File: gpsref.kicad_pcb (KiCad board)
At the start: 4 copper layers, 77.4 x 47.8 mm, 182 parts, among them J1 SMA, J10 Debug, J11 I2C_Snoop, J12 GPS_Snoop, J2 SMA, J3 SMA, J4 SMA, J5 U.Fl, J6 SMA, J7 USB_C_Receptacle_16P, J8 U.Fl, Q1 AO3400A, Q2 AO3401A, T1 MABA-007159-000000, T2 MABA-007159-000000, U1 MAX-M10S, U11 74LVC1G07, U2 LMK05318BRGZR, U21 TMP117xxDRV, U3 TG5032CGN, U31 74LVC1G125, U4 STM32H503KBUx, U41 74CB3Q3306, U5 TPS82084SIL, U6 TPS82084SIL, U7 TPS7A8801RTJR, U8 TPS7A8801RTJR, Y1 32768Hz

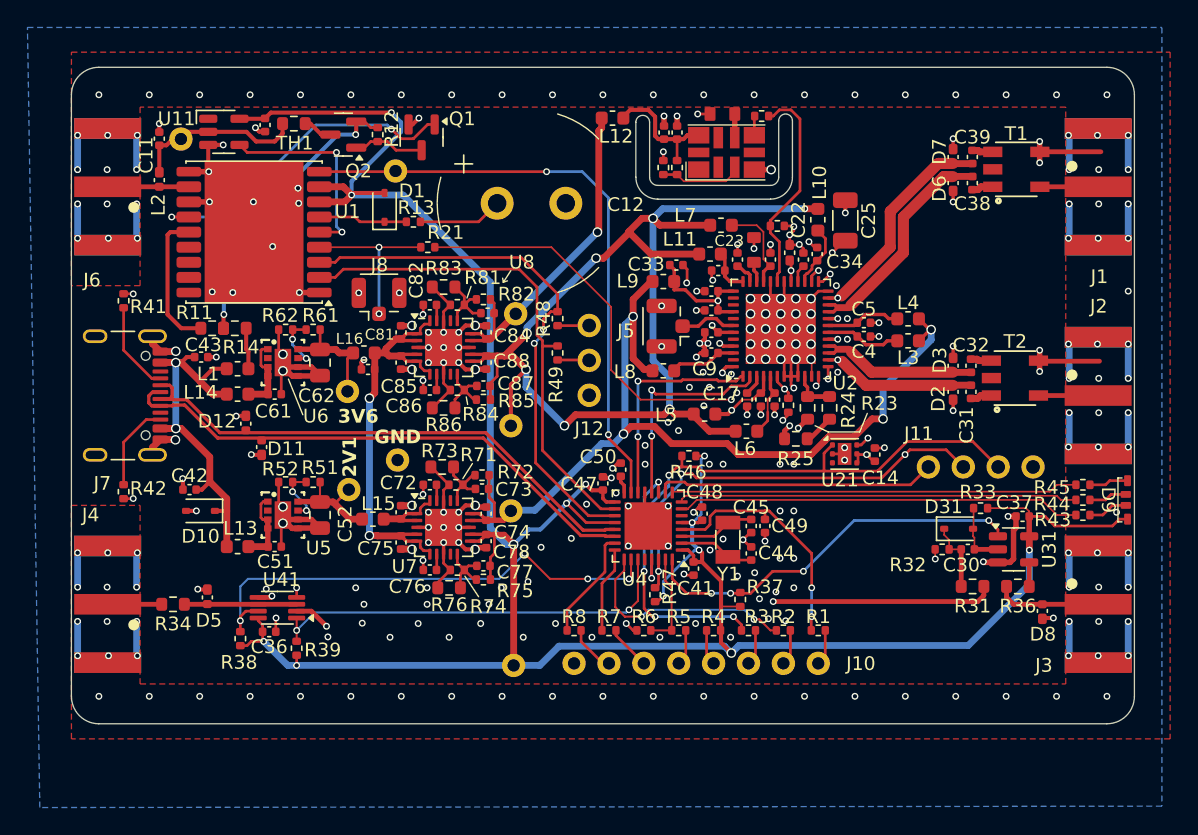
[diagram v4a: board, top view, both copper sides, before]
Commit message: Change the programming connector.
Change the SMA footprint to match narrow ones.
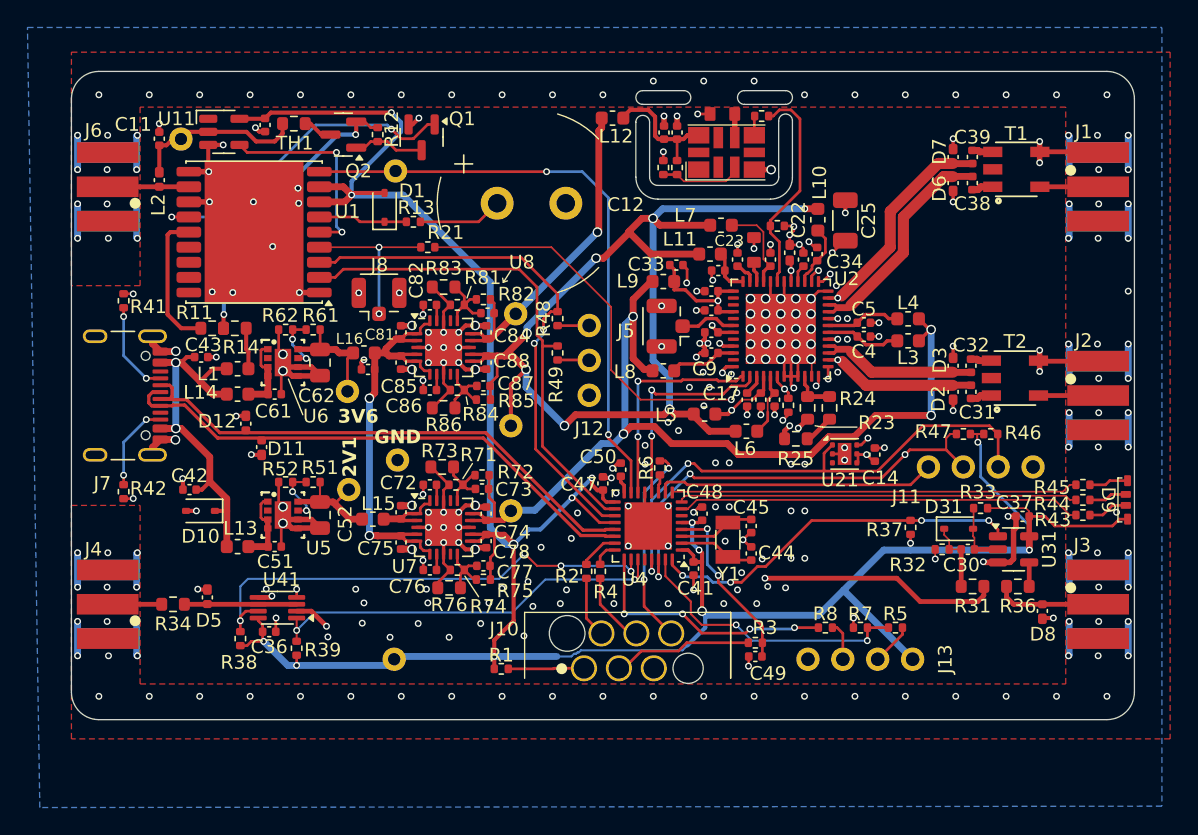
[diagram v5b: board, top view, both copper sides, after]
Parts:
- added J13: Boot, Parts:PinHeader_1x04_P2.54mm_Vertical, F.Cu at (161.2, 119.2)
- J1, J2, J3, J4, J6: footprint Parts:SMA_Amphenol_132289_EdgeMount -> Parts:SMA_EdgeMount
- J10: value Debug -> Skedd; footprint Parts:PinHeader_1x08_P2.54mm_Vertical -> Parts:Skedd6
- moved R47 25.3 mm to (164.9, 102.8), turned to 0 degrees
- moved R1 23.2 mm to (131.3, 119.9)
- moved R46 22.0 mm to (166.9, 102.8), turned to 180 degrees
- moved R7 18.3 mm to (157.4, 116.9)
- moved R8 18.3 mm to (154.9, 116.9)
- moved R5 15.8 mm to (160.0, 116.9)
- moved R2 15.0 mm to (137.5, 112.8), turned to 90 degrees
- moved J10 13.9 mm to (140.5, 118.6), turned to 90 degrees
- moved R37 13.5 mm to (161.1, 109.6)
- moved R6 11.9 mm to (142.8, 105.3), turned to -90 degrees
- moved C49 9.53 mm to (149.8, 119.0), turned to 180 degrees
- moved R4 9.31 mm to (138.5, 112.8), turned to 90 degrees
- moved TP7 8.71 mm to (123.5, 119.2)
- moved R3 1.03 mm to (149.8, 118.0), turned to 0 degrees
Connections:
- J10 pad 1: /CPU/dRST -> /CPU/d3V3
- J10 pad 2: /CPU/dRX -> /CPU/dSWD
- J10 pad 3: /CPU/dTX -> /CPU/dRST
- J10 pad 4: /CPU/d3V3 -> /CPU/dSWC
- J10 pad 5: /CPU/dBOOT -> GND
- J10 pad 6: /CPU/dSWC -> /CPU/dTX
- R1 pad 1: /CPU/dRST -> /CPU/d3V3
- R1 pad 2: /CPU/CPU_nRST -> +3V3
- R2 pad 1: /CPU/dRX -> /CPU/dSWD
- R2 pad 2: /CPU/DBG_RX -> /CPU/SWDIO
- R3 pad 1: /CPU/dTX -> /CPU/dRST
- R3 pad 2: /CPU/DBG_TX -> /CPU/CPU_nRST
- R4 pad 1: /CPU/d3V3 -> /CPU/dSWC
- R4 pad 2: +3V3 -> /CPU/SWCLK
- R6 pad 1: /CPU/BOOT0 -> /CPU/dTX
- R6 pad 2: GND -> /CPU/DBG_TX
- R7 pad 1: /CPU/dSWC -> /CPU/BOOT0
- R7 pad 2: /CPU/SWCLK -> GND
- R8 pad 1: /CPU/dSWD -> /CPU/dRX
- R8 pad 2: /CPU/SWDIO -> /CPU/DBG_RX
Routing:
- net +3V3: track 197.3 -> 232.6 mm, vias 13 -> 14
- net /CPU/DBG_TX: track 18.4 -> 1.32 mm, vias 4 -> 0
- net /CPU/BOOT0: track 6.82 -> 20.9 mm, vias 0 -> 2
- net /CPU/dTX: track 1.89 -> 14.7 mm, vias 0 -> 2
- net /CPU/dRST: track 1.89 -> 9.82 mm
- net /CPU/SWDIO: track 8.12 -> 2.87 mm
- net /CPU/CPU_nRST: track 17.9 -> 12.8 mm
- net /CPU/SWCLK: track 6.24 -> 1.84 mm
- net /CPU/d3V3: track 2.70 -> 5.53 mm
- net /CPU/DBG_RX: track 16.6 -> 18.8 mm, vias 2 -> 4
- net CGEN_1V8: track 66.7 -> 68.6 mm
- net /CPU/dSWC: track 3.24 -> 4.89 mm
- net SecRef: track 51.6 -> 50.0 mm
- net /CPU/dSWD: track 3.06 -> 4.46 mm
- net EN_OUT3: track 28.5 -> 27.3 mm
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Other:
- board size 77.4 x 47.8 mm -> 77.4 x 47.2 mm

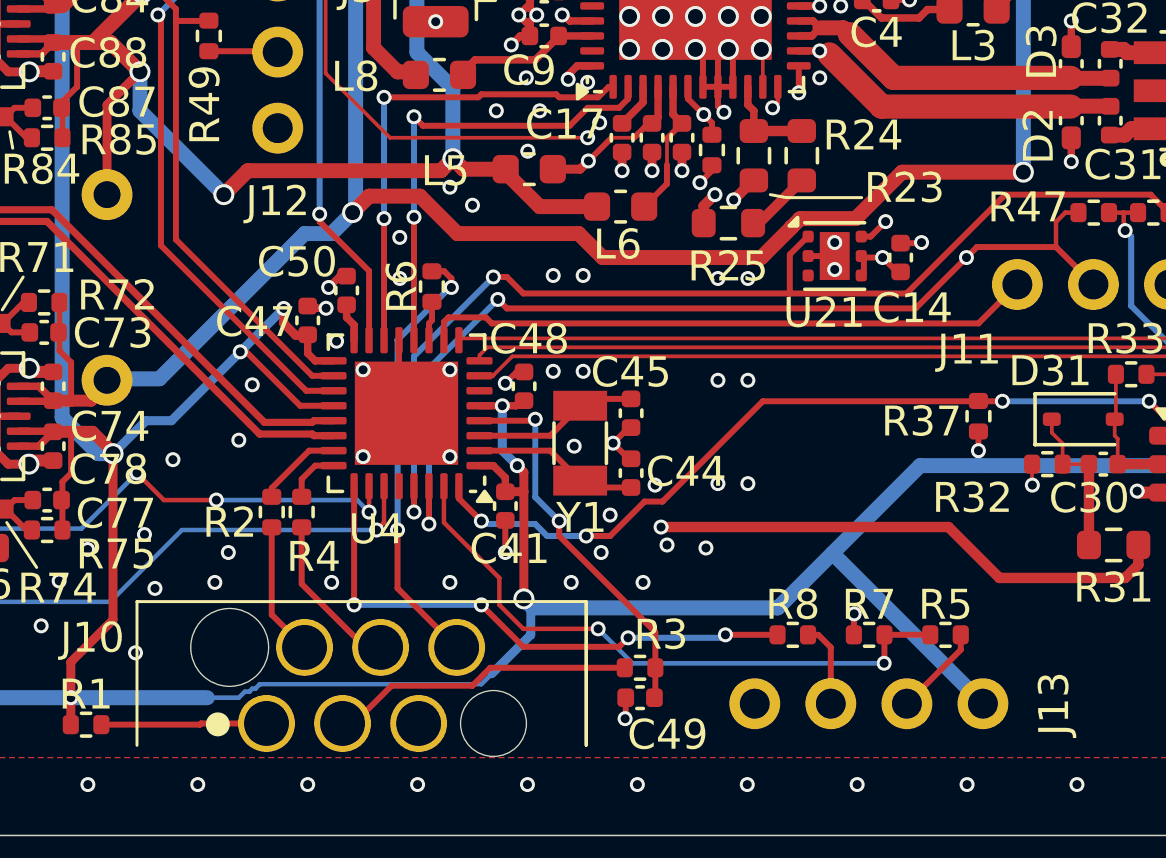
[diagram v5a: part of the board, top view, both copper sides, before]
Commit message: Tidy up pinout.
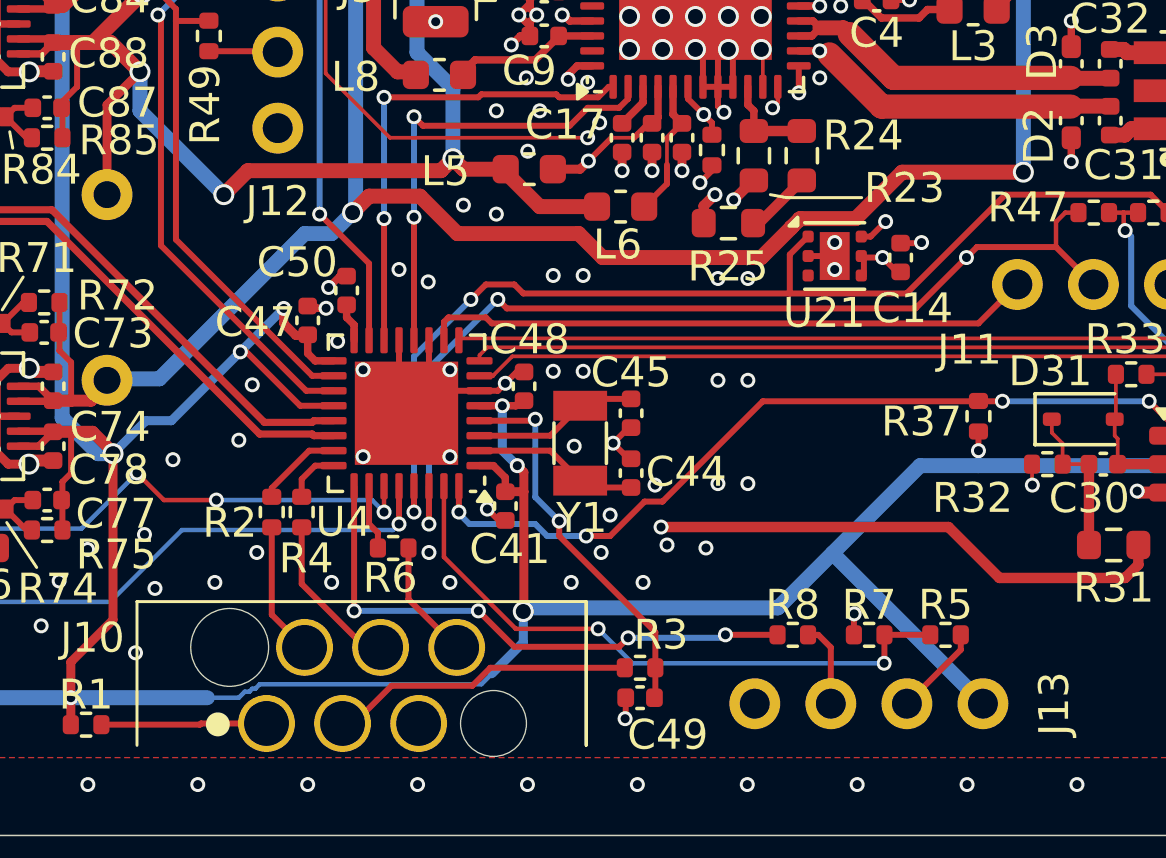
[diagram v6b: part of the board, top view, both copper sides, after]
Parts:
- moved R6 8.83 mm to (141.6, 114.0), turned to 180 degrees
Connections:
- U4 pad 11: /CPU/DBG_TX -> GND
- U4 pad 26: EN_OUT4 -> /CPU/DBG_TX
- U4 pad 27: EN_REF2 -> EN_OUT4
- U4 pad 28: unconnected-(U4-PB5-Pad28) -> EN_REF2
- U4 pad 6: unconnected-(U4-PA0-Pad6) -> GND
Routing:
- net /CPU/dTX: track 14.7 -> 3.99 mm, vias 2 -> 0
- net GND: track 214.1 -> 219.2 mm, vias 303 -> 304
- net /CPU/DBG_TX: track 1.32 -> 2.18 mm
- net +3V3: track 232.6 -> 232.0 mm
- net OUT4: track 43.9 -> 44.5 mm
- net EN_REF2: track 29.4 -> 29.9 mm
- net EN_OUT4: track 35.9 -> 36.4 mm

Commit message: Ready for respin.
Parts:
- moved L12 1.40 mm to (140.8, 79.8)
- moved R27 0.72 mm to (151.0, 87.0), turned to 0 degrees
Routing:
- net +3V3: track 232.0 -> 225.0 mm
- net /Clocking/VCC_XO: track 9.21 -> 6.98 mm
- net GND: track 219.2 -> 217.5 mm
- net TCXO_3V3: track 25.2 -> 26.2 mm
- net /Clocking/XO_P: track 15.8 -> 14.9 mm
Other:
- outline, holes or cut-outs redrawn
- board text added: "1V8"
- board text added: "3V3"
- board text added: "CG3V3"

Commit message: Schematic updates for revision mostly done.
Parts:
- moved J7 1.20 mm to (101.6, 100.0)
- moved R41 1.20 mm to (102.6, 93.1)
- moved R42 1.20 mm to (102.6, 107.0)
- moved D9 1.20 mm to (178.1, 107.6)
- moved R43 1.10 mm to (174.8, 108.7)
- moved R44 1.10 mm to (174.8, 107.6)
- moved R45 1.10 mm to (174.8, 106.5)
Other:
- board size 77.4 x 47.2 mm -> 79.8 x 47.2 mm
